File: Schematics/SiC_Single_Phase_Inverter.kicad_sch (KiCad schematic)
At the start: 0 parts

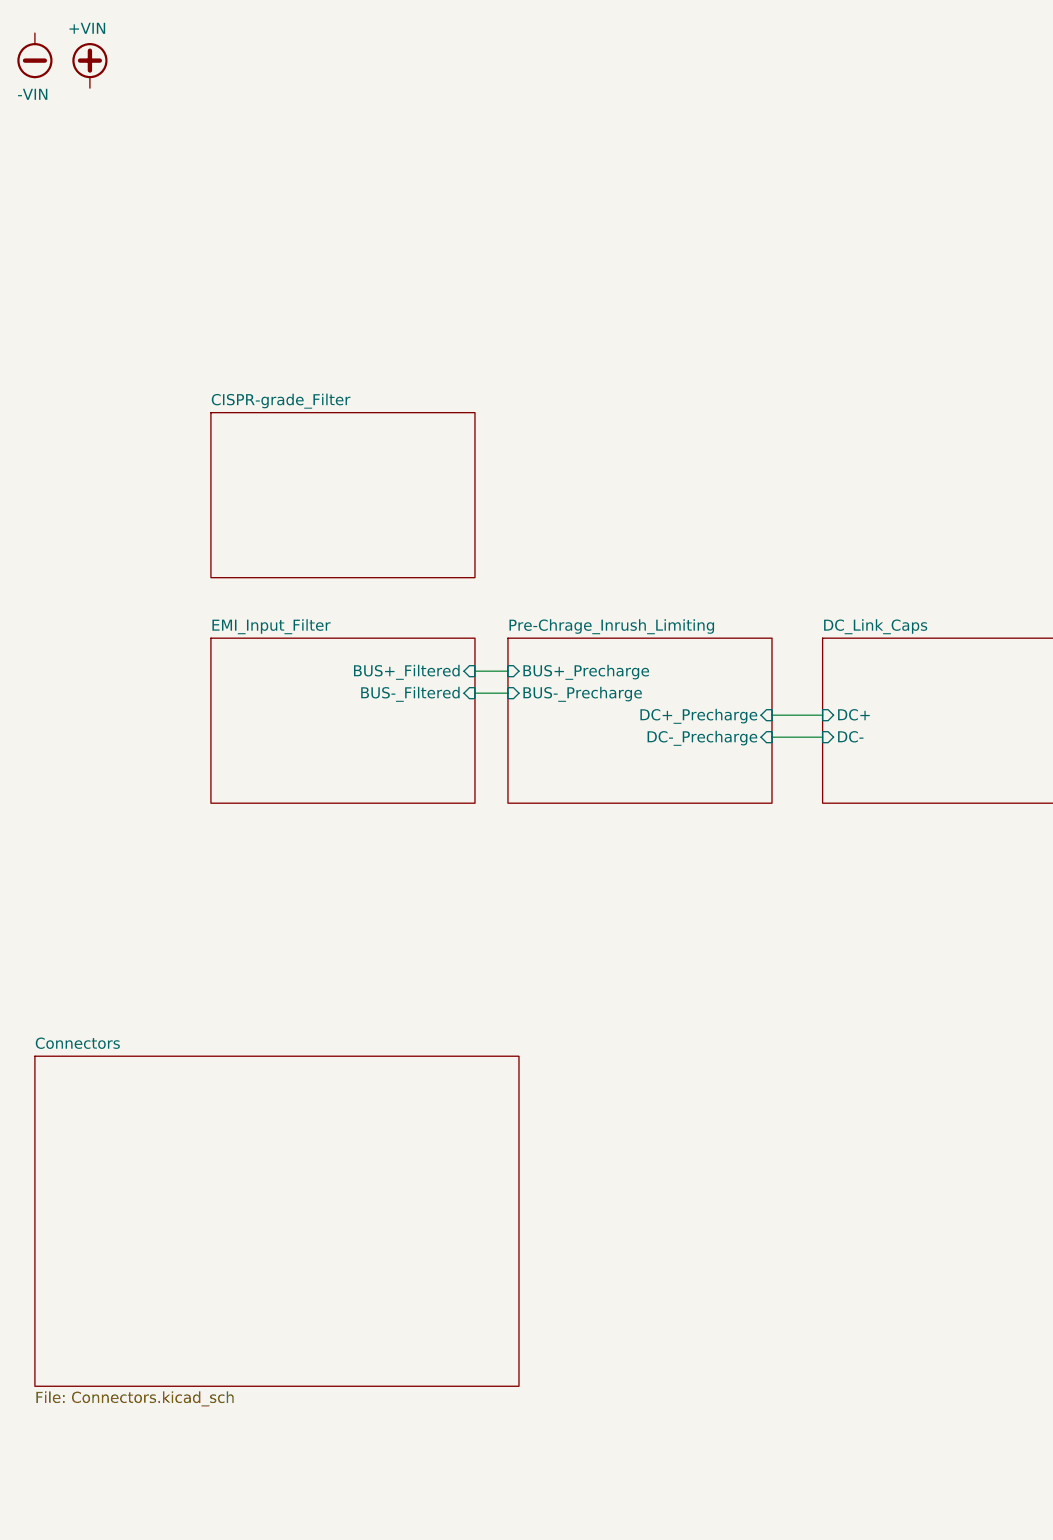
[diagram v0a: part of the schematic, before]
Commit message: [SiC Inverter WIP]
- Deleted backup files
- changed symbol and footprint lib locations
- added text discription explaining the DC link sub sheet and emi  input
  filter subsheet
- Added Vin+,- Black and Red connector
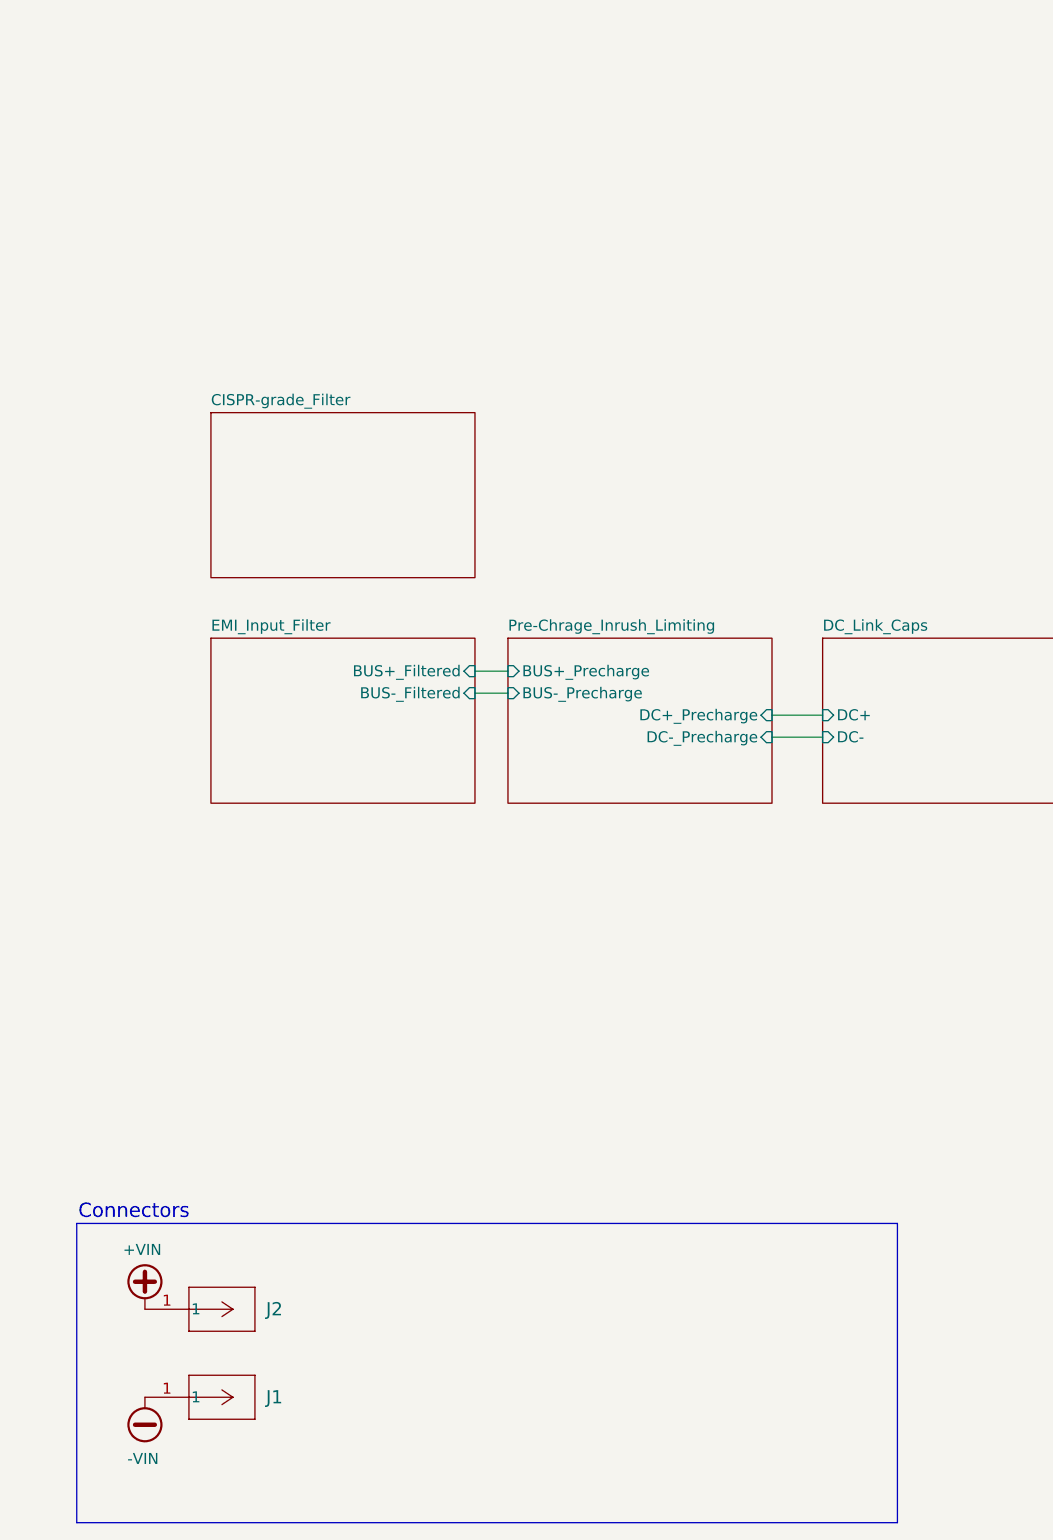
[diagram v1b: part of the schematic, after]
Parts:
- added J1: 23AH8785-Black, SiC_Inverter:23AH8785-Black, symbol SiC_Inverter:23AH8785-Black
- added J2: 23AH8786-Red, SiC_Inverter:23AH8786-Red, symbol SiC_Inverter:23AH8786-Red
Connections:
- net +VIN: now also J2.1
- net -VIN: now also J1.1
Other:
- removed sheet Connectors
- note added: "Connectors"
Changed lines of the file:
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@@
 	(generator_version "9.0")
 	(paper "A4")
+	(rectangle
+		(start 26.416 152.654)
+		(end 121.158 187.198)
+		(stroke
+			(width 0)
+			(type default)
+		)
+		(fill
+			(type none)
+		)
+	)
+	(text "Connectors"
+		(exclude_from_sim no)
+		(at 33.02 151.384 0)
+		(effects
+			(font
+				(size 1.651 1.651)
+			)
+		)
+	)
 	(wire
 		(pts
@@
 	)
 	(symbol
+		(lib_id "SiC_Inverter:23AH8785-Black")
+		(at 34.29 172.72 0)
+		(unit 1)
+		(exclude_from_sim no)
+		(in_bom yes)
+		(on_board yes)
+		(dnp no)
+		(fields_autoplaced yes)
+		(property "Reference" "J1"
+			(at 48.26 172.7199 0)
+			(effects
+				(font
+					(size 1.524 1.524)
+				)
+				(justify left)
+			)
+		)
+		(property "Value" "23AH8785-Black"
+			(at 46.482 181.61 0)
+			(effects
+				(font
+					(size 1.524 1.524)
+				)
+				(hide yes)
+			)
+		)
+		(property "Footprint" "SiC_Inverter:23AH8785-Black"
+			(at 50.546 177.546 0)
+			(effects
+				(font
+					(size 1.27 1.27)
+					(italic yes)
+				)
+				(hide yes)
+			)
+		)
+		(property "Datasheet" "https://www.farnell.com/datasheets/3945771.pdf"
+			(at 63.5 179.578 0)
+			(effects
+				(font
+					(size 1.27 1.27)
+					(italic yes)
+				)
+				(hide yes)
+			)
+		)
+		(property "Description" "Black:The 66.9040-22 is an 4mm Angled Socket for mounting on PCBs, gold-plated brass contact terminal."
+			(at 89.916 183.642 0)
+			(effects
+				(font
+					(size 1.27 1.27)
+				)
+				(hide yes)
+			)
+		)
+		(pin "1"
+		)
+		(instances
+			(project "SiC_Single_Phase_Inverter"
+				(path "/a1ed0539-9735-4ad1-a8fd-87e26e7fce16"
+					(reference "J1")
+					(unit 1)
+				)
+			)
+		)
+	)
+	(symbol
 		(lib_id "power:+VDC")
-		(at 27.94 21.59 0)
+		(at 34.29 162.56 0)
 		(unit 1)
 		(exclude_from_sim no)
@@
 		(dnp no)
 		(property "Reference" "#PWR05"
-			(at 27.94 24.13 0)
+			(at 34.29 165.1 0)
 			(effects
 				(font
@@
 		)
 		(property "Value" "+VIN"
-			(at 25.4 14.732 0)
+			(at 31.75 155.702 0)
 			(effects
 				(font
@@
 		)
 		(property "Footprint" ""
-			(at 27.94 21.59 0)
+			(at 34.29 162.56 0)
 			(effects
 				(font
@@
 		)
 		(property "Datasheet" ""
-			(at 27.94 21.59 0)
+			(at 34.29 162.56 0)
 			(effects
 				(font
@@
 		)
 		(property "Description" "Power symbol creates a global label with name \"+VDC\""
-			(at 27.94 21.59 0)
+			(at 34.29 162.56 0)
 			(effects
 				(font
@@
 	)
 	(symbol
+		(lib_id "SiC_Inverter:23AH8786-Red")
+		(at 34.29 162.56 0)
+		(unit 1)
+		(exclude_from_sim no)
+		(in_bom yes)
+		(on_board yes)
+		(dnp no)
+		(fields_autoplaced yes)
+		(property "Reference" "J2"
+			(at 48.26 162.5599 0)
+			(effects
+				(font
+					(size 1.524 1.524)
+				)
+				(justify left)
+			)
+		)
+		(property "Value" "23AH8786-Red"
+			(at 45.974 171.45 0)
+			(effects
+				(font
+					(size 1.524 1.524)
+				)
+				(hide yes)
+			)
+		)
+		(property "Footprint" "SiC_Inverter:23AH8786-Red"
+			(at 51.816 167.386 0)
+			(effects
+				(font
+					(size 1.27 1.27)
+					(italic yes)
+				)
+				(hide yes)
+			)
+		)
+		(property "Datasheet" "https://www.farnell.com/datasheets/3945771.pdf"
+			(at 64.262 169.418 0)
+			(effects
+				(font
+					(size 1.27 1.27)
+					(italic yes)
+				)
+				(hide yes)
+			)
+		)
+		(property "Description" "Red: The 66.9040-22 is an 4mm Angled Socket for mounting on PCBs, gold-plated brass contact terminal."
+			(at 92.964 173.482 0)
+			(effects
+				(font
+					(size 1.27 1.27)
+				)
+				(hide yes)
+			)
+		)
+		(pin "1"
+		)
+		(instances
+			(project "SiC_Single_Phase_Inverter"
+				(path "/a1ed0539-9735-4ad1-a8fd-87e26e7fce16"
+					(reference "J2")
+					(unit 1)
+				)
+			)
+		)
+	)
+	(symbol
 		(lib_id "power:-VDC")
-		(at 21.59 15.24 180)
+		(at 34.29 172.72 180)
 		(unit 1)
 		(exclude_from_sim no)
@@
 		(dnp no)
 		(property "Reference" "#PWR01"
-			(at 21.59 12.7 0)
+			(at 34.29 170.18 0)
 			(effects
 				(font
@@
 		)
 		(property "Value" "-VIN"
-			(at 19.558 22.352 0)
+			(at 32.258 179.832 0)
 			(effects
 				(font
@@
 		)
 		(property "Footprint" ""
-			(at 21.59 15.24 0)
+			(at 34.29 172.72 0)
 			(effects
 				(font
@@
 		)
 		(property "Datasheet" ""
-			(at 21.59 15.24 0)
+			(at 34.29 172.72 0)
 			(effects
 				(font
@@
 		)
 		(property "Description" "Power symbol creates a global label with name \"-VDC\""
-			(at 21.59 15.24 0)
+			(at 34.29 172.72 0)
 			(effects
 				(font
@@
 				)
 			)
-		)
-	)
-	(sheet
-		(at 21.59 133.35)
-		(size 55.88 38.1)
-		(exclude_from_sim no)
-		(in_bom yes)
-		(on_board yes)
-		(dnp no)
-		(fields_autoplaced yes)
-		(stroke
-			(width 0.1524)
-			(type solid)
-		)
-		(fill
-			(color 0 0 0 0.0000)
-		)
-		(property "Sheetname" "Connectors"
-			(at 21.59 132.6384 0)
-			(effects
-				(font
-					(size 1.27 1.27)
-				)
-				(justify left bottom)
-			)
-		)
-		(property "Sheetfile" "Connectors.kicad_sch"
-			(at 21.59 172.0346 0)
-			(effects
-				(font
-					(size 1.27 1.27)
-				)
-				(justify left top)
-			)
-		)
-		(instances
-			(project "SiC_Single_Phase_Inverter"
-				(path "/a1ed0539-9735-4ad1-a8fd-87e26e7fce16"
-					(page "8")
-				)
-			)

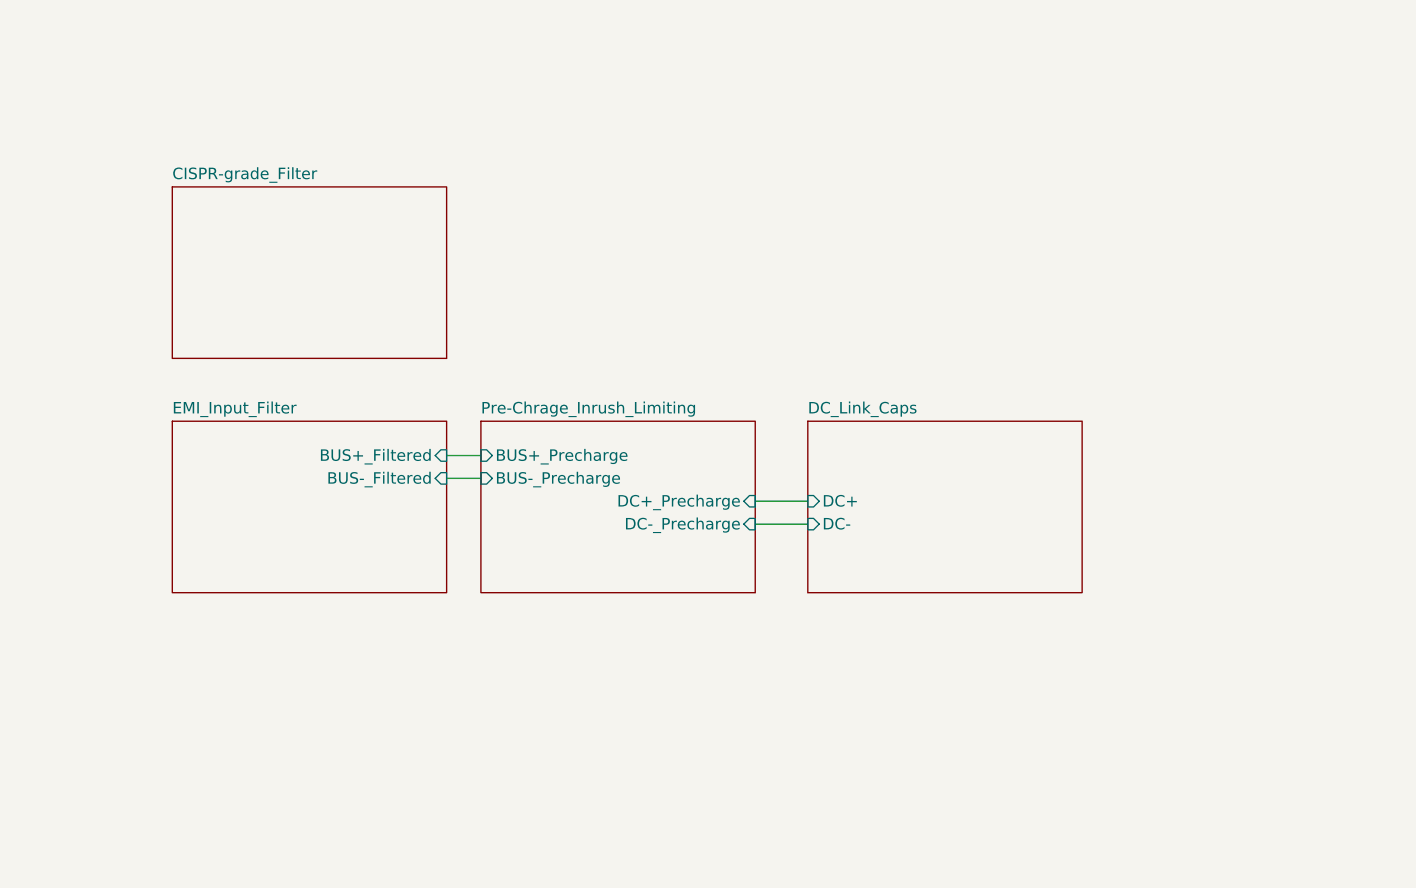
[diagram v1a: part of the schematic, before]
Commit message: Work in progress
- Added new parts to PCB to check 3d models
- Added input protection sheet
- Added TVS, N-Channel MOSFET, Zensor, and resiters to protection
  circuit
- Added datasheets for new parts
- Added circuit GND
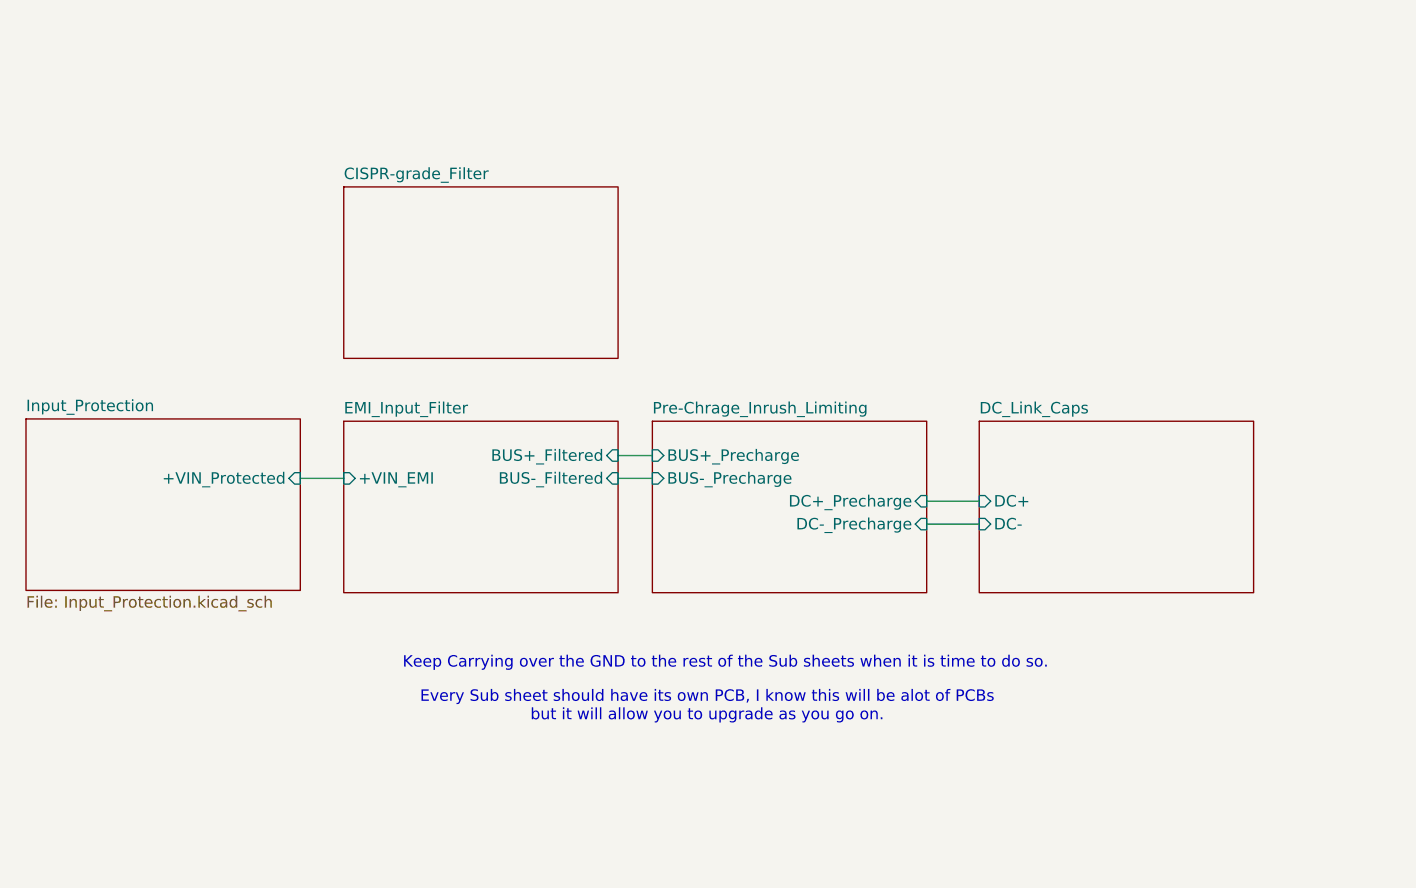
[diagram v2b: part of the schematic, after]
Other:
- added sheet Input_Protection (Input_Protection.kicad_sch)
- sheet EMI_Input_Filter ports: added +VIN_EMI; removed none
- note added: "Every Sub sheet should have its own PCB, I know this will be alot of PCBs but it will allow you to upgrade as you go on."
- note added: "Keep Carrying over the GND to the rest of the Sub sheets when it is time to do so."
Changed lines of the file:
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@@
+		)
+	)
+	(text "Every Sub sheet should have its own PCB, I know this will be alot of PCBs\nbut it will allow you to upgrade as you go on.\n"
+		(exclude_from_sim no)
+		(at 101.346 116.84 0)
+		(effects
+			(font
+				(size 1.27 1.27)
+			)
+		)
+	)
+	(text "Keep Carrying over the GND to the rest of the Sub sheets when it is time to do so. \n"
+		(exclude_from_sim no)
+		(at 103.378 112.014 0)
+		(effects
+			(font
+				(size 1.27 1.27)
+			)
 		)
 	)
@@
 	(wire
 		(pts
-			(xy 72.39 88.9) (xy 76.2 88.9)
+			(xy 91.44 88.9) (xy 95.25 88.9)
 		)
 		(stroke
@@
 	(wire
 		(pts
-			(xy 106.68 93.98) (xy 112.522 93.98)
+			(xy 125.73 93.98) (xy 131.572 93.98)
 		)
 		(stroke
@@
 	(wire
 		(pts
-			(xy 72.39 91.44) (xy 76.2 91.44)
+			(xy 56.134 91.44) (xy 60.96 91.44)
 		)
 		(stroke
@@
 	(wire
 		(pts
-			(xy 106.68 96.52) (xy 112.522 96.52)
+			(xy 91.44 91.44) (xy 95.25 91.44)
+		)
+		(stroke
+			(width 0)
+			(type default)
+		)
+	)
+	(wire
+		(pts
+			(xy 125.73 96.52) (xy 131.572 96.52)
 		)
 		(stroke
@@
 	)
 	(sheet
-		(at 76.2 85.09)
+		(at 95.25 85.09)
 		(size 30.48 19.05)
 		(exclude_from_sim no)
@@
 		)
 		(property "Sheetname" "Pre-Chrage_Inrush_Limiting"
-			(at 76.2 84.3784 0)
+			(at 95.25 84.3784 0)
 			(effects
 				(font
@@
 		)
 		(property "Sheetfile" "Pre-Chrage_Inrush_Limiting.kicad_sch"
-			(at 76.2 104.7246 0)
+			(at 95.25 104.7246 0)
 			(effects
 				(font
@@
 		)
 		(pin "BUS+_Precharge" input
-			(at 76.2 88.9 180)
+			(at 95.25 88.9 180)
 			(effects
 				(font
@@
 		)
 		(pin "BUS-_Precharge" input
-			(at 76.2 91.44 180)
+			(at 95.25 91.44 180)
 			(effects
 				(font
@@
 		)
 		(pin "DC+_Precharge" input
-			(at 106.68 93.98 0)
+			(at 125.73 93.98 0)
 			(effects
 				(font
@@
 		)
 		(pin "DC-_Precharge" input
-			(at 106.68 96.52 0)
+			(at 125.73 96.52 0)
 			(effects
 				(font
@@
 	)
 	(sheet
-		(at 41.91 85.09)
+		(at 60.96 85.09)
 		(size 30.48 19.05)
 		(exclude_from_sim no)
@@
 		)
 		(property "Sheetname" "EMI_Input_Filter"
-			(at 41.91 84.3784 0)
+			(at 60.96 84.3784 0)
 			(effects
 				(font
@@
 		)
 		(property "Sheetfile" "EMI_Input_Filter.kicad_sch"
-			(at 41.91 104.7246 0)
+			(at 60.96 104.7246 0)
 			(effects
 				(font
@@
 		)
 		(pin "BUS+_Filtered" input
-			(at 72.39 88.9 0)
+			(at 91.44 88.9 0)
 			(effects
 				(font
@@
 		)
 		(pin "BUS-_Filtered" input
-			(at 72.39 91.44 0)
+			(at 91.44 91.44 0)
 			(effects
 				(font
@@
 				)
 				(justify right)
+			)
+		)
+		(pin "+VIN_EMI" input
+			(at 60.96 91.44 180)
+			(effects
+				(font
+					(size 1.27 1.27)
+				)
+				(justify left)
 			)
 		)
@@
 	)
 	(sheet
-		(at 41.91 59.055)
+		(at 60.96 59.055)
 		(size 30.48 19.05)
 		(exclude_from_sim no)
@@
 		)
 		(property "Sheetname" "CISPR‑grade_Filter"
-			(at 41.91 58.3434 0)
+			(at 60.96 58.3434 0)
 			(effects
 				(font
@@
 		)
 		(property "Sheetfile" "CISPR‑grade_Filter.kicad_sch"
-			(at 41.91 78.6896 0)
+			(at 60.96 78.6896 0)
 			(effects
 				(font
@@
 	)
 	(sheet
-		(at 112.522 85.09)
+		(at 131.572 85.09)
 		(size 30.48 19.05)
 		(exclude_from_sim no)
@@
 		)
 		(property "Sheetname" "DC_Link_Caps"
-			(at 112.522 84.3784 0)
+			(at 131.572 84.3784 0)
 			(effects
 				(font
@@
 		)
 		(property "Sheetfile" "DC_Link_Caps.kicad_sch"
-			(at 112.522 104.7246 0)
+			(at 131.572 104.7246 0)
 			(effects
 				(font
@@
 		)
 		(pin "DC+" input
-			(at 112.522 93.98 180)
+			(at 131.572 93.98 180)
 			(effects
 				(font
@@
 		)
 		(pin "DC-" input
-			(at 112.522 96.52 180)
+			(at 131.572 96.52 180)
 			(effects
 				(font
@@
 				)
 			)
+		)
+	)
+	(sheet
+		(at 25.654 84.836)
+		(size 30.48 19.05)
+		(exclude_from_sim no)
+		(in_bom yes)
+		(on_board yes)
+		(dnp no)
+		(fields_autoplaced yes)
+		(stroke
+			(width 0.1524)
+			(type solid)
+		)
+		(fill
+			(color 0 0 0 0.0000)
+		)
+		(property "Sheetname" "Input_Protection"
+			(at 25.654 84.1244 0)
+			(effects
+				(font
+					(size 1.27 1.27)
+				)
+				(justify left bottom)
+			)
+		)
+		(property "Sheetfile" "Input_Protection.kicad_sch"
+			(at 25.654 104.4706 0)
+			(effects
+				(font
+					(size 1.27 1.27)
+				)
+				(justify left top)
+			)
+		)
+		(pin "+VIN_Protected" input
+			(at 56.134 91.44 0)
+			(effects
+				(font
+					(size 1.27 1.27)
+				)
+				(justify right)
+			)
+		)
+		(instances
+			(project "SiC_Single_Phase_Inverter"
+				(path "/a1ed0539-9735-4ad1-a8fd-87e26e7fce16"
+					(page "11")
+				)
+			)
